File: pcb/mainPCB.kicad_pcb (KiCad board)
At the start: 4 copper layers, 160 x 73.2 mm, 161 parts, among them IC1 FXL6408UMX, IC2 ATA6561-GAQW-N, IC3 ICL3221EIVZ, J1 PTSM-Header-Horizontal-6, J10 Conn_01x08_Female, J11 Conn_01x08_Female, J12 Conn_02x02_Odd_Even, J13 SM04B-SRSS-TB(LF)(SN), J14 USB_B_Micro, J15 RJ45_Amphenol_RJMG1BD3B8K1ANR, J16 DB9_Male_MountingHoles, J17 SM04B-SRSS-TB(LF)(SN), J18 PTSM-Header-Horizontal-2, J3 PTSM-Header-Horizontal-7, J4 CCA-Header-Horizontal-4, J5 PTSM-Header-Horizontal-5, J7 Conn_01x04_Male, J8 Conn_01x04_Male, J9 Conn_01x08_Female, K1 CP1SA-12V-Z, K2 CP1SA-12V-Z, Q1 BC817-40,215, Q2 BC817-40,215, SW1 SW_Push, U1 ESP32-WROOM-32, U10 NUD3124LT1G, U11 LAN8720A, U12 LSM9DS1, U2 AZ1117-3.3, U3 VNH7070AS, U4 ADS1115IDGS, U5 VNH7070AS, U6 PCA9306DCTR, U7 TPD3E001DRLR, U8 CP2102N-A01-GQFN24, U9 VNH7070AS

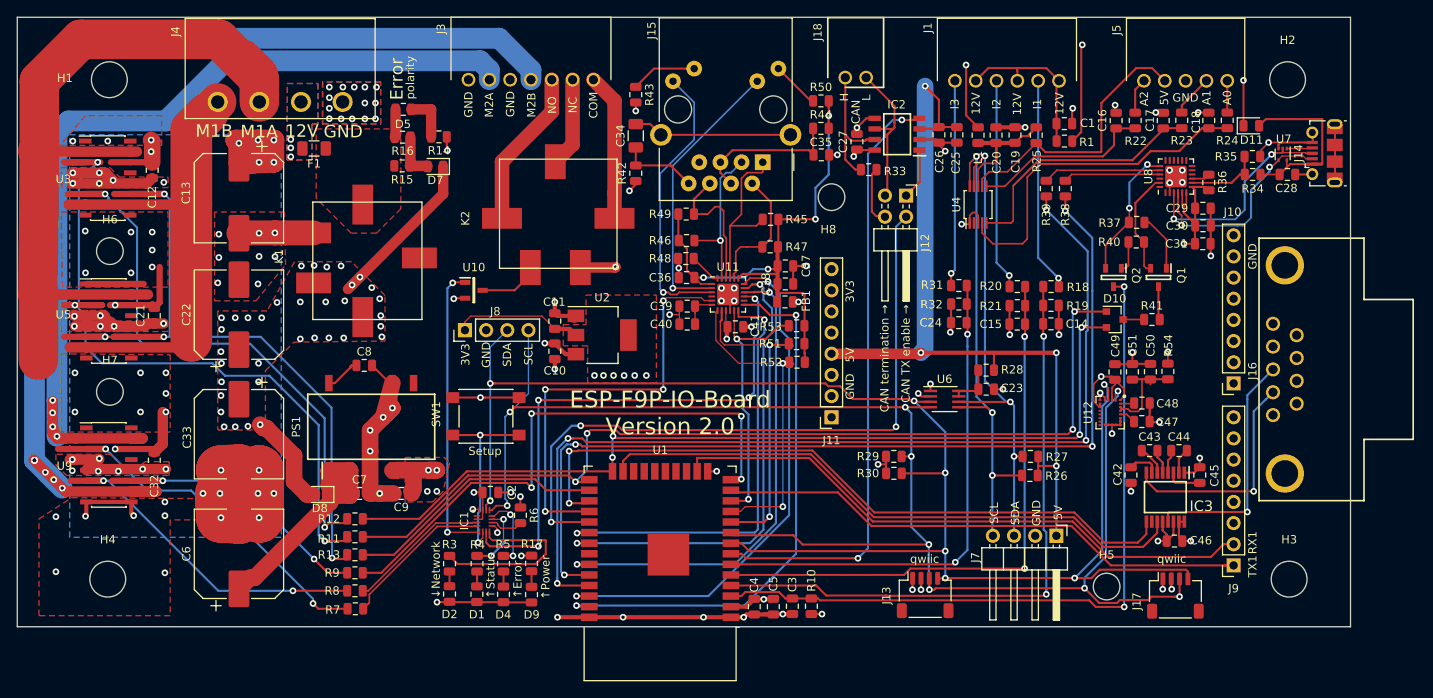
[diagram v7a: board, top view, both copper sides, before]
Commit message: Added five fiducials. fixes #3
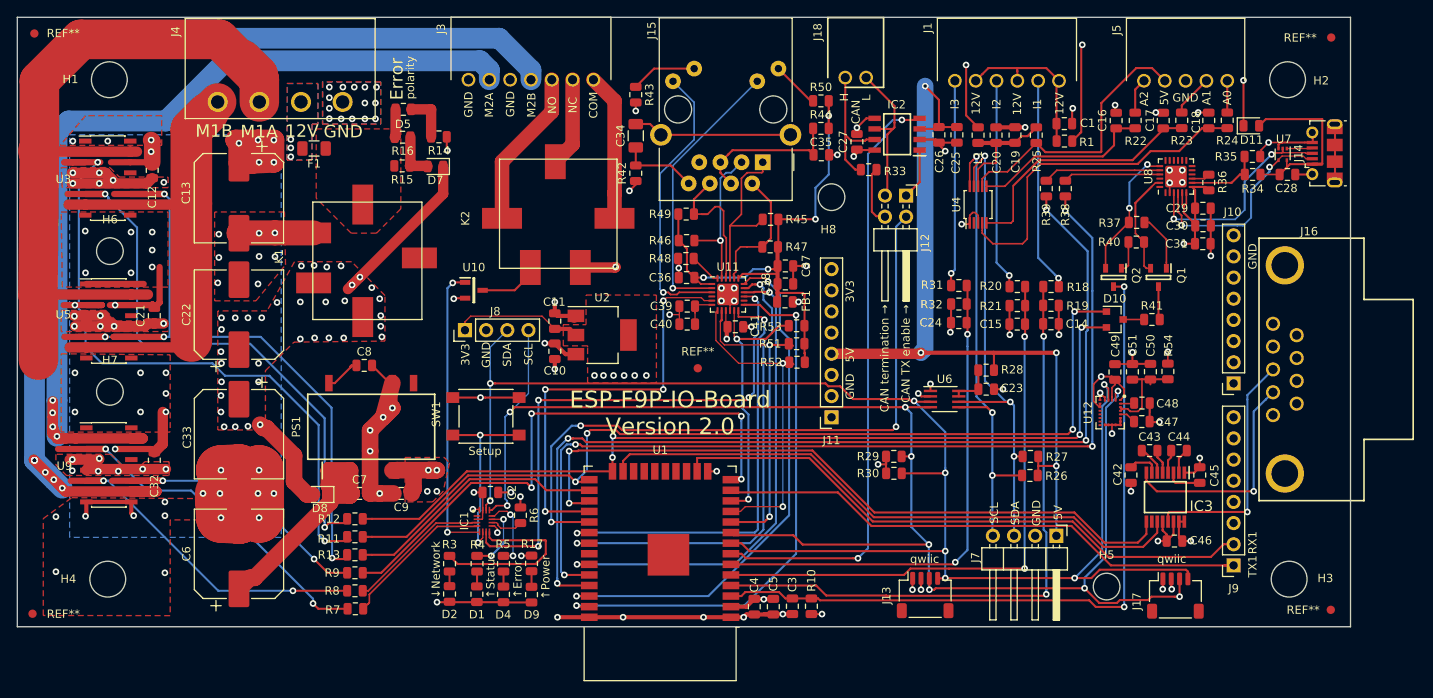
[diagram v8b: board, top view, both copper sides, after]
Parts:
- added ?: , , F.Cu at (16.0, 41.7)
- added REF**: Fiducial_1mm_Dia_2mm_Outer, Fiducial:Fiducial_1mm_Dia_2mm_Outer, F.Cu at (19.5, 39.4)
- added REF**: Fiducial_1mm_Dia_2mm_Outer, Fiducial:Fiducial_1mm_Dia_2mm_Outer, F.Cu at (19.3, 109.1)
- added REF**: Fiducial_1mm_Dia_2mm_Outer, Fiducial:Fiducial_1mm_Dia_2mm_Outer, F.Cu at (175.1, 108.6)
- added REF**: Fiducial_1mm_Dia_2mm_Outer, Fiducial:Fiducial_1mm_Dia_2mm_Outer, F.Cu at (175.2, 39.9)
- added REF**: Fiducial_1mm_Dia_2mm_Outer, Fiducial:Fiducial_1mm_Dia_2mm_Outer, F.Cu at (99.1, 79.6)
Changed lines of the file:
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@@
     (tracks 1805)
     (zones 0)
-    (modules 161)
+    (modules 167)
     (nets 181)
   )
@@
     (add_net /powerSupply/V_In_12V)
   )
+  (module "" (layer F.Cu)
+    (at 15.9512 41.74744)
+    (fp_text reference "" (at 53.083 53.213) (layer F.SilkS)
+      (effects (font (size 1.27 1.27) (thickness 0.15)))
+    )
+    (fp_text value "" (at 53.083 53.213) (layer F.SilkS)
+      (effects (font (size 1.27 1.27) (thickness 0.15)))
+    )
+    (fp_text user %R (at -107.83616 61.66104) (layer F.Fab)
+      (effects (font (size 0.4 0.4) (thickness 0.06)))
+    )
+  )
   (module ICs_own:Fuse_1206_3216Metric (layer F.Cu)
     (at 53.083 53.213 180)
@@
     (descr LD09P33E4GV00LF)
     (tags Connector)
-    (fp_text reference J16 (at -0.1905 -13.3731 90) (layer F.SilkS)
+    (fp_text reference J16 (at 16.5608 -6.58876 180) (layer F.SilkS)
       (effects (font (size 1 1) (thickness 0.154)))
     )
@@
     (tags "mounting hole 4.3mm no annular m4 din965")
     (attr virtual)
-    (fp_text reference H3 (at 0 -4.75) (layer F.SilkS)
+    (fp_text reference H3 (at 4.34594 -0.10668) (layer F.SilkS)
       (effects (font (size 1 1) (thickness 0.15)))
     )
@@
     (tags "mounting hole 4.3mm no annular m4 din965")
     (attr virtual)
-    (fp_text reference H4 (at 0 -4.75) (layer F.SilkS)
+    (fp_text reference H4 (at -4.73456 -0.02032) (layer F.SilkS)
       (effects (font (size 1 1) (thickness 0.15)))
     )
@@
     (tags "mounting hole 4.3mm no annular m4 din965")
     (attr virtual)
-    (fp_text reference H1 (at -5.334 -0.1905) (layer F.SilkS)
+    (fp_text reference H1 (at -4.67106 -0.05588) (layer F.SilkS)
       (effects (font (size 1 1) (thickness 0.15)))
     )
@@
     (tags "mounting hole 4.3mm no annular m4 din965")
     (attr virtual)
-    (fp_text reference H2 (at 0 -4.75) (layer F.SilkS)
+    (fp_text reference H2 (at 4.02844 0.11176) (layer F.SilkS)
       (effects (font (size 1 1) (thickness 0.15)))
     )
@@
     )
   )
+  (module Fiducial:Fiducial_1mm_Dia_2mm_Outer (layer F.Cu)
+    (at 19.51228 39.41064)
+    (descr "Circular Fiducial, 1mm bare copper top, 2mm keepout (Level A)")
+    (tags fiducial)
+    (attr smd)
+    (fp_text reference REF** (at 3.46964 -0.02032) (layer F.SilkS)
+      (effects (font (size 1 1) (thickness 0.15)))
+    )
+    (fp_text value Fiducial_1mm_Dia_2mm_Outer (at 0 2) (layer F.Fab)
+      (effects (font (size 1 1) (thickness 0.15)))
+    )
+    (fp_circle (center 0 0) (end 1.25 0) (layer F.CrtYd) (width 0.05))
+    (fp_text user %R (at 0 0) (layer F.Fab)
+      (effects (font (size 0.4 0.4) (thickness 0.06)))
+    )
+    (fp_circle (center 0 0) (end 1 0) (layer F.Fab) (width 0.1))
+    (pad "" smd circle (at 0 0) (size 1 1) (layers F.Cu F.Mask)
+      (solder_mask_margin 0.5) (clearance 0.5))
+  )
+  (module Fiducial:Fiducial_1mm_Dia_2mm_Outer (layer F.Cu)
+    (at 19.28876 109.05236)
+    (descr "Circular Fiducial, 1mm bare copper top, 2mm keepout (Level A)")
+    (tags fiducial)
+    (attr smd)
+    (fp_text reference REF** (at 3.69824 0.03048) (layer F.SilkS)
+      (effects (font (size 1 1) (thickness 0.15)))
+    )
+    (fp_text value Fiducial_1mm_Dia_2mm_Outer (at 0 2) (layer F.Fab)
+      (effects (font (size 1 1) (thickness 0.15)))
+    )
+    (fp_circle (center 0 0) (end 1.25 0) (layer F.CrtYd) (width 0.05))
+    (fp_text user %R (at 0 0) (layer F.Fab)
+      (effects (font (size 0.4 0.4) (thickness 0.06)))
+    )
+    (fp_circle (center 0 0) (end 1 0) (layer F.Fab) (width 0.1))
+    (pad "" smd circle (at 0 0) (size 1 1) (layers F.Cu F.Mask)
+      (solder_mask_margin 0.5) (clearance 0.5))
+  )
+  (module Fiducial:Fiducial_1mm_Dia_2mm_Outer (layer F.Cu)
+    (at 175.11268 108.585)
+    (descr "Circular Fiducial, 1mm bare copper top, 2mm keepout (Level A)")
+    (tags fiducial)
+    (attr smd)
+    (fp_text reference REF** (at -3.31724 0.01524) (layer F.SilkS)
+      (effects (font (size 1 1) (thickness 0.15)))
+    )
+    (fp_text value Fiducial_1mm_Dia_2mm_Outer (at 0 2) (layer F.Fab)
+      (effects (font (size 1 1) (thickness 0.15)))
+    )
+    (fp_circle (center 0 0) (end 1.25 0) (layer F.CrtYd) (width 0.05))
+    (fp_text user %R (at 0 0) (layer F.Fab)
+      (effects (font (size 0.4 0.4) (thickness 0.06)))
+    )
+    (fp_circle (center 0 0) (end 1 0) (layer F.Fab) (width 0.1))
+    (pad "" smd circle (at 0 0) (size 1 1) (layers F.Cu F.Mask)
+      (solder_mask_margin 0.5) (clearance 0.5))
+  )
+  (module Fiducial:Fiducial_1mm_Dia_2mm_Outer (layer F.Cu)
+    (at 175.16348 39.89324)
+    (descr "Circular Fiducial, 1mm bare copper top, 2mm keepout (Level A)")
+    (tags fiducial)
+    (attr smd)
+    (fp_text reference REF** (at -3.71856 0.03048) (layer F.SilkS)
+      (effects (font (size 1 1) (thickness 0.15)))
+    )
+    (fp_text value Fiducial_1mm_Dia_2mm_Outer (at 0 2) (layer F.Fab)
+      (effects (font (size 1 1) (thickness 0.15)))
+    )
+    (fp_circle (center 0 0) (end 1.25 0) (layer F.CrtYd) (width 0.05))
+    (fp_text user %R (at 0 0) (layer F.Fab)
+      (effects (font (size 0.4 0.4) (thickness 0.06)))
+    )
+    (fp_circle (center 0 0) (end 1 0) (layer F.Fab) (width 0.1))
+    (pad "" smd circle (at 0 0) (size 1 1) (layers F.Cu F.Mask)
+      (solder_mask_margin 0.5) (clearance 0.5))
+  )
+  (module Fiducial:Fiducial_1mm_Dia_2mm_Outer (layer F.Cu)
+    (at 99.1362 79.58836)
+    (descr "Circular Fiducial, 1mm bare copper top, 2mm keepout (Level A)")
+    (tags fiducial)
+    (attr smd)
+    (fp_text reference REF** (at 0 -2) (layer F.SilkS)
+      (effects (font (size 1 1) (thickness 0.15)))
+    )
+    (fp_text value Fiducial_1mm_Dia_2mm_Outer (at 0 2) (layer F.Fab)
+      (effects (font (size 1 1) (thickness 0.15)))
+    )
+    (fp_circle (center 0 0) (end 1.25 0) (layer F.CrtYd) (width 0.05))
+    (fp_text user %R (at 0 0) (layer F.Fab)
+      (effects (font (size 0.4 0.4) (thickness 0.06)))
+    )
+    (fp_circle (center 0 0) (end 1 0) (layer F.Fab) (width 0.1))
+    (pad "" smd circle (at 0 0) (size 1 1) (layers F.Cu F.Mask)
+      (solder_mask_margin 0.5) (clearance 0.5))
+  )
   (gr_text 3V3 (at 117.4115 70.358 90) (layer F.SilkS)
     (effects (font (size 1 1) (thickness 0.2)))
@@
       (pts
         (xy 24.003 95.123) (xy 41.656 95.25) (xy 41.656 97.79) (xy 35.814 97.79) (xy 35.814 109.2835)
-        (xy 20.066 109.2835) (xy 20.066 97.663)
+        (xy 20.57908 109.25937) (xy 20.57908 97.63887)
       )
     )
